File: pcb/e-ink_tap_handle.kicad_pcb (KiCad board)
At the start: 2 copper layers, 61.5 x 31.5 mm, 42 parts, among them IC1 MDBT42Q-512KV2, IC2 LSM6DSLTR, J1 JTAG_SWD_6, J2 USB_C_Receptacle_USB2.0, J3 Conn_01x24, Q1 2N7002E, U1 TP4056, U2 XC6206PxxxMR

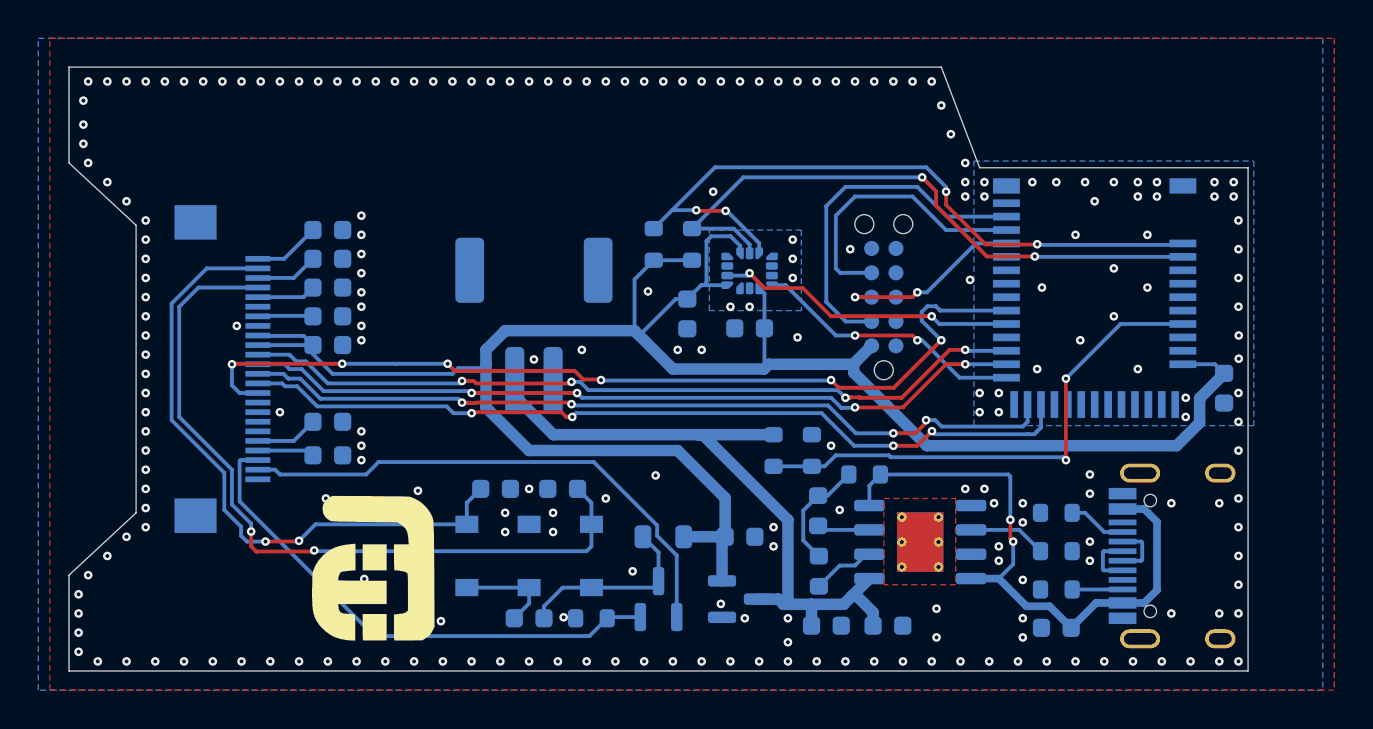
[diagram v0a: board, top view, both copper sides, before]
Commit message: mall changes to PCB 3v3 routing
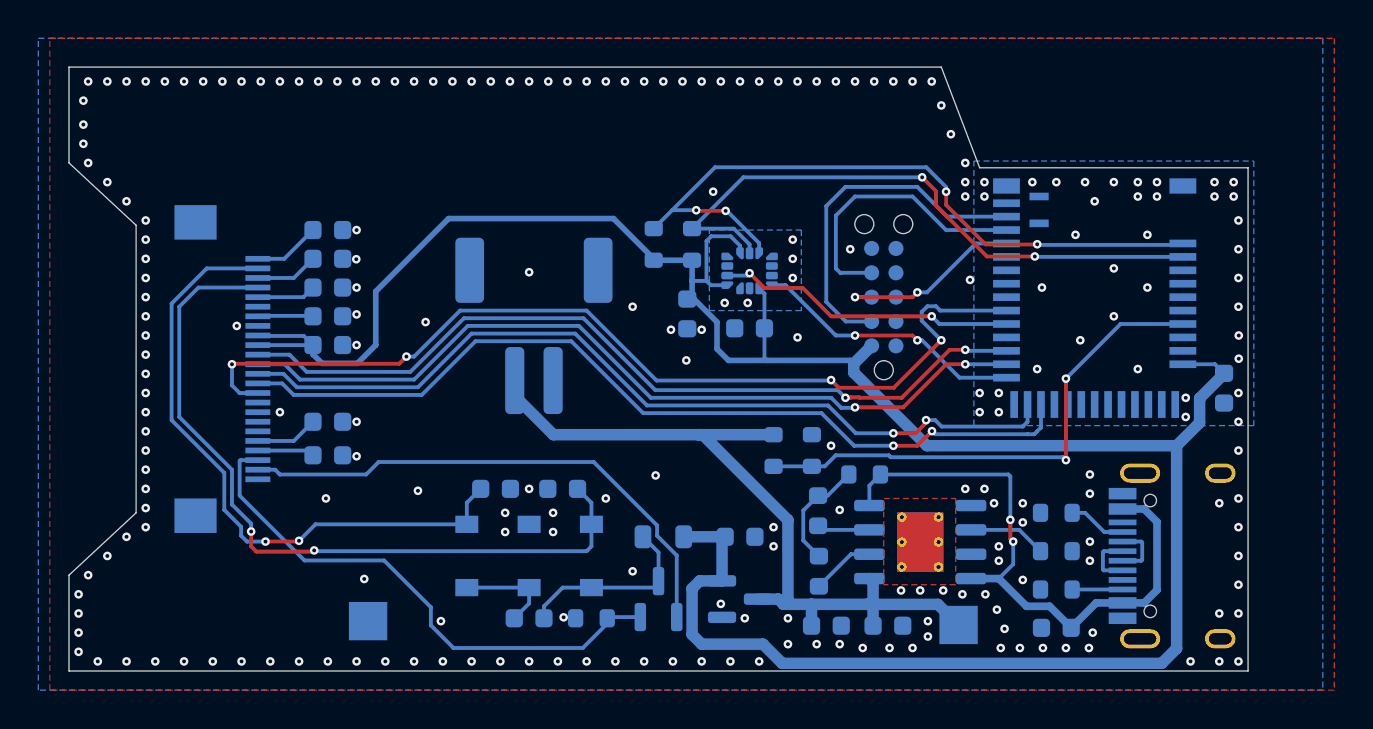
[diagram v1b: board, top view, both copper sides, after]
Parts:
- removed Ref**: Val**, Acea:aces_electronics_small
- added TP1: B+, TestPoint:TestPoint_Pad_2.0x2.0mm, B.Cu at (185.4, 108.6)
- added TP2: B-, TestPoint:TestPoint_Pad_2.0x2.0mm, B.Cu at (154.6, 108.4)
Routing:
- net +3V3: track 108.9 -> 128.7 mm
- net Net-(BT1-+): track 35.9 -> 41.2 mm
- net SCK: track 40.9 -> 43.3 mm, vias 4 -> 2
- net eRESET: track 47.7 -> 50.0 mm, vias 6 -> 4
- net CS: track 43.0 -> 45.3 mm, vias 4 -> 2
- net MOSI: track 41.2 -> 43.4 mm, vias 4 -> 2
- net DC: track 44.1 -> 46.2 mm, vias 4 -> 2
- net RESE: track 27.3 -> 28.3 mm
- net GND: vias 233 -> 230
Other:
- board text added: "B+"
- board text added: "B-"
